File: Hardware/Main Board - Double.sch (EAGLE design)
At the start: 69 parts, among them J1 MICROMOD-2222-C, J10 MICRO-SD-PUSH-PUSH-EXT-PIN, J2 Vertical Qwiic Connector, J4 QWIIC_RIGHT_ANGLE, J5 CORTEX_JTAG_DEBUG_MINIMUM_PTH, J6 MICROMOD_CARRIER, J7 MICROMOD_CARRIER, Q1 3.1A/30V/105mΩ, U2 MCP73831, U5 AP7361C-33

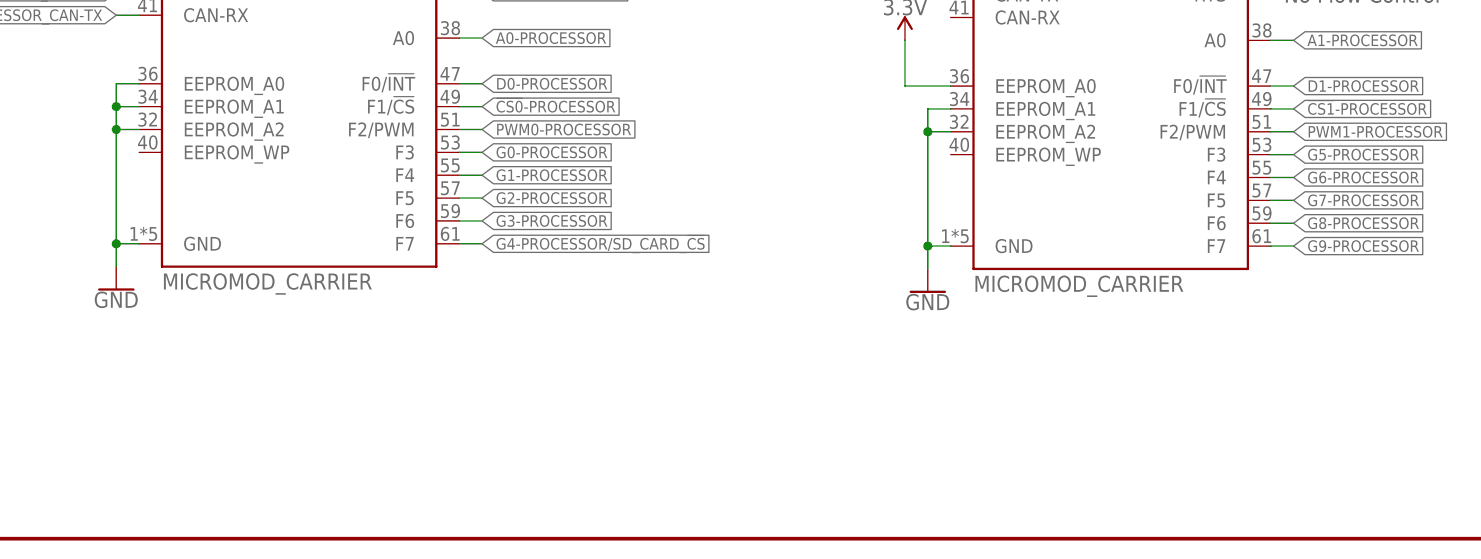
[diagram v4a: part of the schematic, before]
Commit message: Updates the design to use the Micromod-function device in the official SFE Eagle Libs
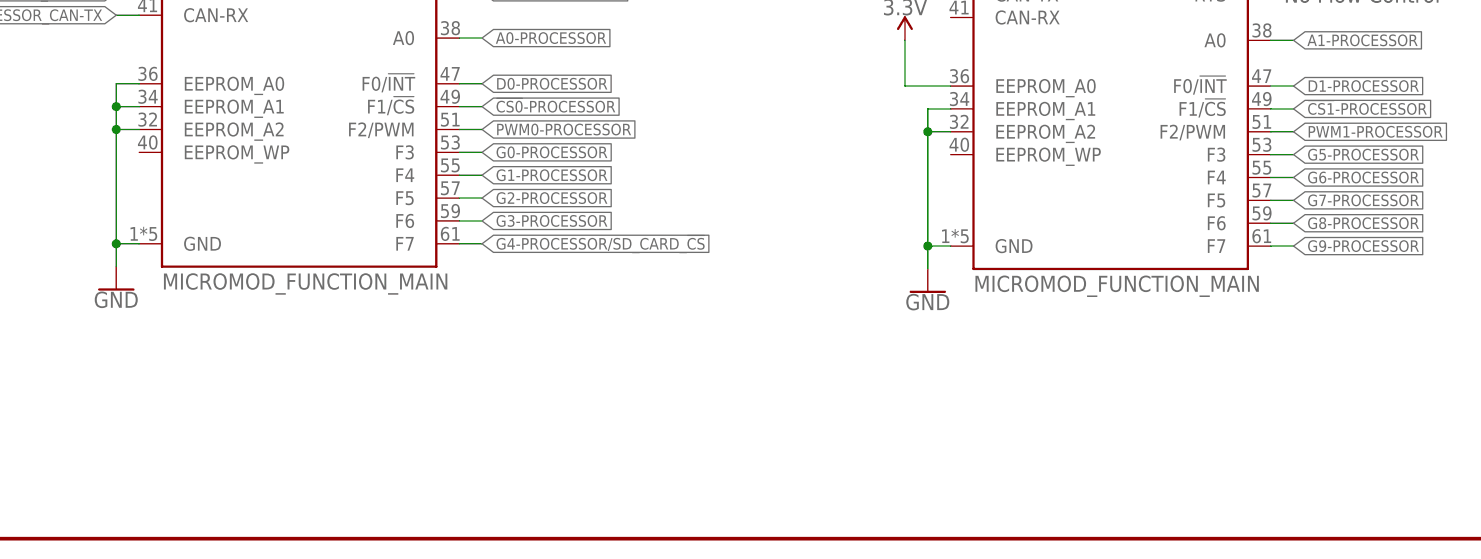
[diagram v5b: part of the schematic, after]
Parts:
- J6, J7: value MICROMOD_CARRIER -> MICROMOD_FUNCTION_MAIN; device SparkFun-MicroMod-Function:MICROMOD_CARRIER -> SparkFun-MicroMod:MICROMOD_FUNCTION_MAIN
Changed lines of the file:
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@@
 <?xml version="1.0" encoding="utf-8"?>
 <!DOCTYPE eagle SYSTEM "eagle.dtd">
-<eagle version="9.6.2">
+<eagle version="9.5.1">
 <drawing>
 <settings>
@@
 <part name="R10" library="SparkFun-Resistors" deviceset="20KOHM" device="-0603-1/10W-1%" value="20k"/>
 <part name="GND23" library="SparkFun-PowerSymbols" deviceset="GND" device=""/>
-<part name="J6" library="SparkFun-MicroMod-Function" deviceset="MICROMOD" device="_CARRIER" value="MICROMOD_CARRIER"/>
-<part name="J7" library="SparkFun-MicroMod-Function" deviceset="MICROMOD" device="_CARRIER" value="MICROMOD_CARRIER"/>
+<part name="J6" library="SparkFun-MicroMod" deviceset="MICROMOD_FUNCTION" device="_MAIN" value="MICROMOD_FUNCTION_MAIN"/>
+<part name="J7" library="SparkFun-MicroMod" deviceset="MICROMOD_FUNCTION" device="_MAIN" value="MICROMOD_FUNCTION_MAIN"/>
 <part name="SUPPLY2" library="SparkFun-PowerSymbols" deviceset="3.3V" device=""/>
 <part name="J10" library="SparkFun-Connectors" deviceset="MICRO-SD" device="-PUSH-PUSH-EXT-PIN"/>

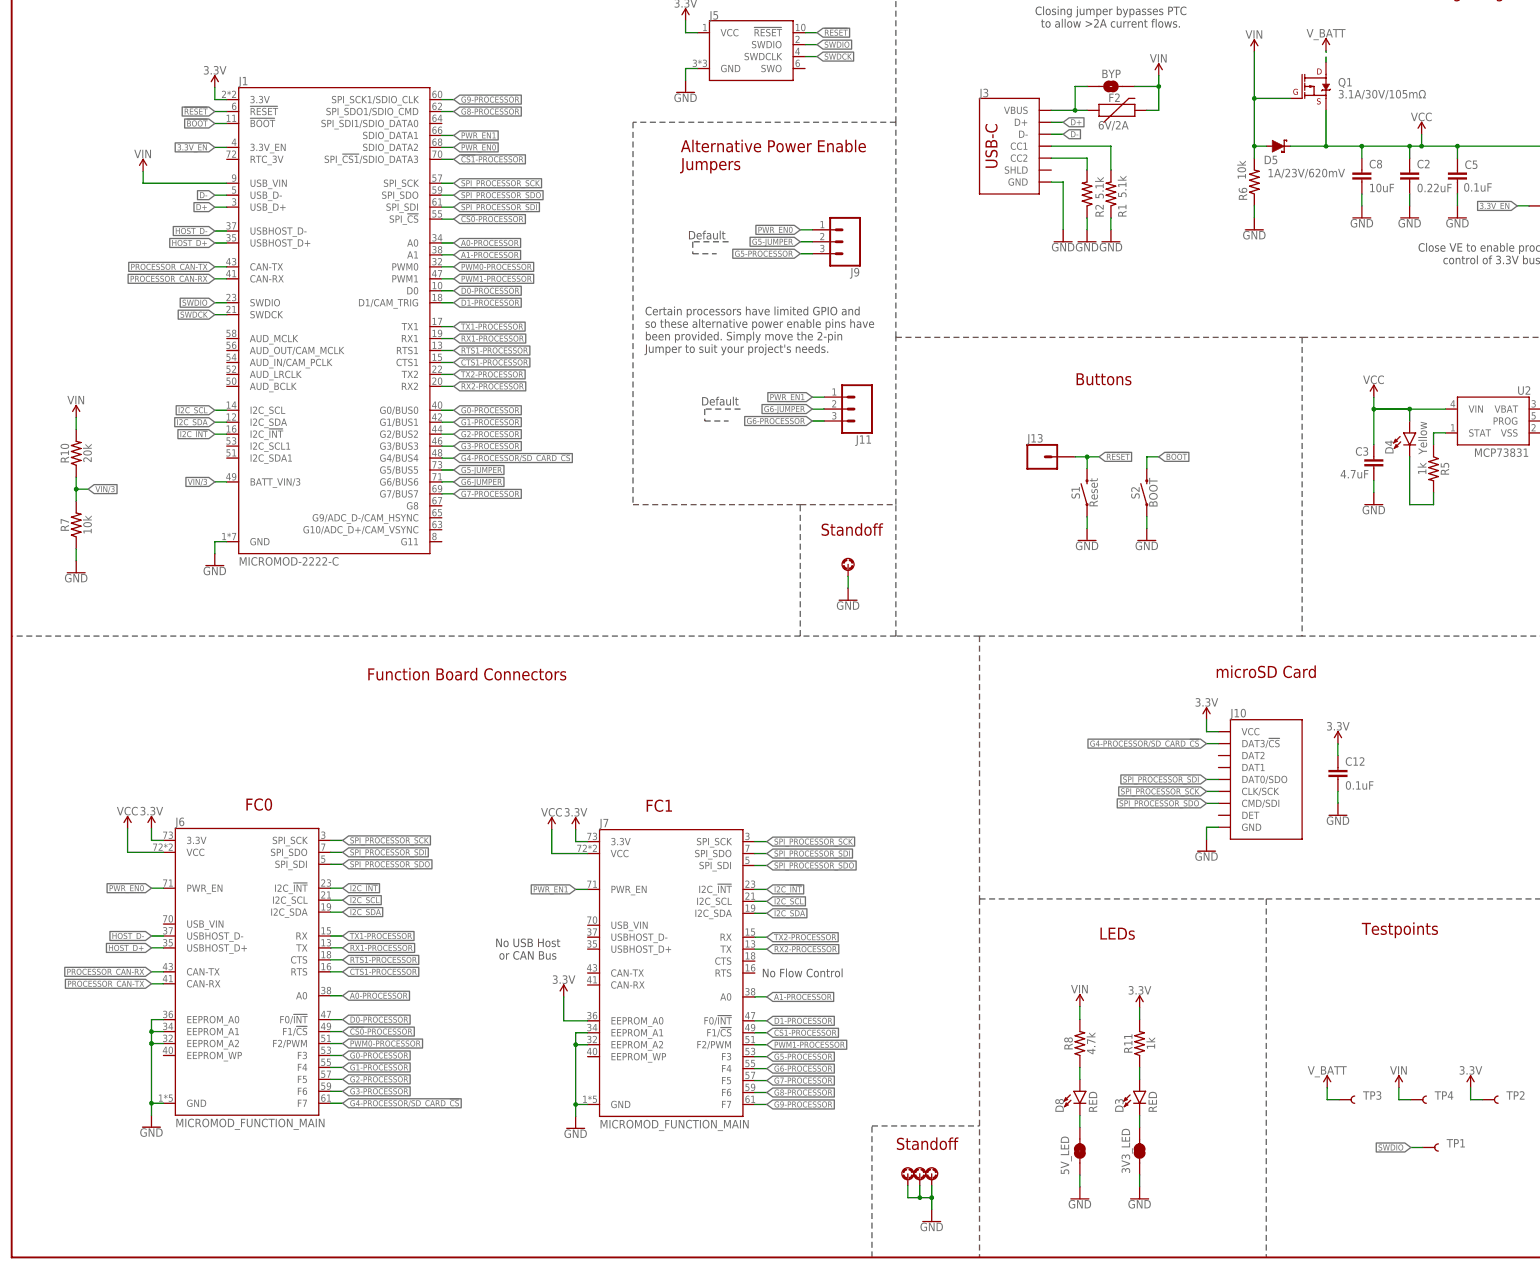
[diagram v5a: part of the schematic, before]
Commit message: Changes resistor values on LEDs, updates plexing symbol, increases capacitor value on microSD
* Adds NC jumper to shield pin on USB-C
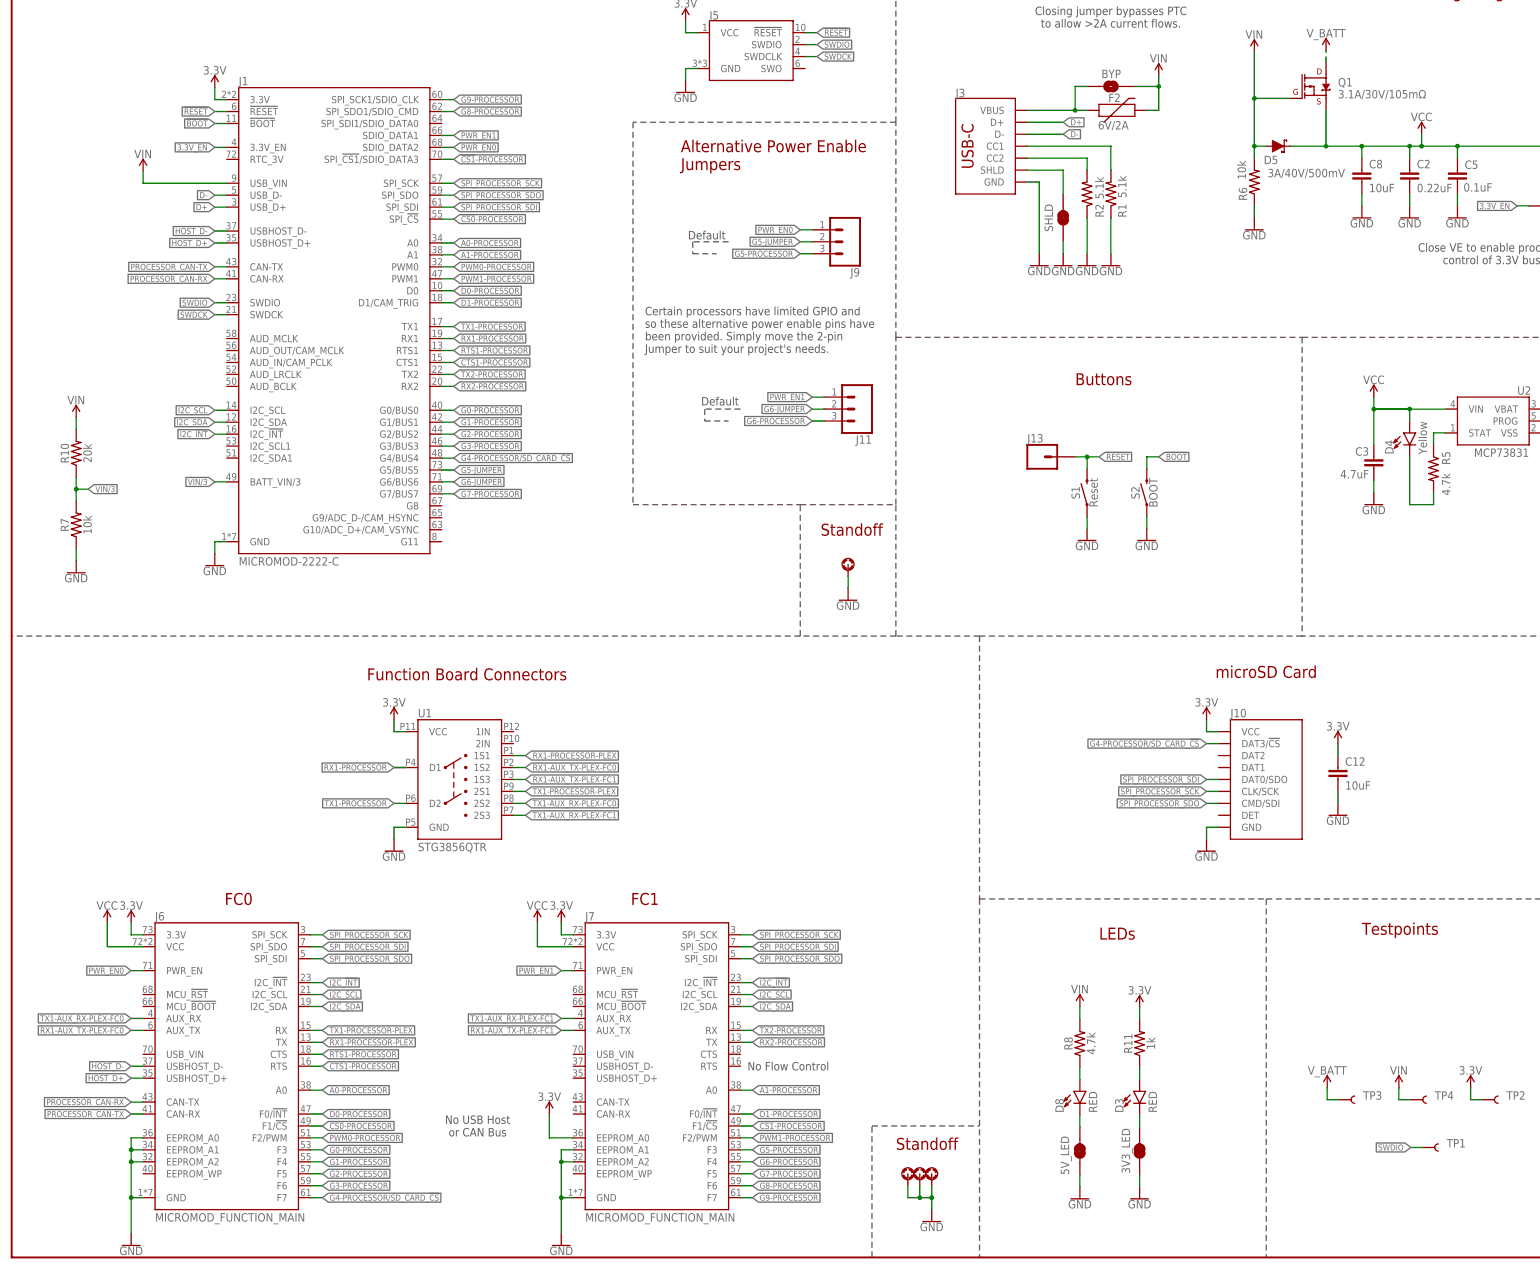
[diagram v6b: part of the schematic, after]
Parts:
- added SHLD: JUMPER-SMT_2_NC_TRACE_SILK, SparkFun-Jumpers:JUMPER-SMT_2_NC_TRACE_SILK
- added U1: STG3856QTR, dip_switch:STG3856QTR
- C12: value 0.1uF -> 10uF; device SparkFun-Capacitors:0.1UF-0603-25V-(+80/-20%) -> SparkFun-Capacitors:10UF-0603-6.3V-20%
- D5: value 1A/23V/620mV -> 3A/40V/500mV; device SparkFun-DiscreteSemi:DIODE-SCHOTTKY-BAT20J -> SparkFun-DiscreteSemi:DIODE-SCHOTTKY-B340A
- R5: value 1k -> 4.7k; device SparkFun-Resistors:1KOHM-0603-1/10W-1% -> SparkFun-Resistors:4.7KOHM-0603-1/10W-1%
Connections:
- new net N$11: J3.SHLD, SHLD.2
- new net N$16: U1.1IN
- new net N$17: U1.2IN
- new net RX1-AUX_TX-PLEX-FC0: J6.AUX_TX, U1.1S2
- new net RX1-AUX_TX-PLEX-FC1: J7.AUX_TX, U1.1S3
- new net RX1-PROCESSOR-PLEX: J6.TX, U1.1S1
- new net TX1-AUX_RX-PLEX-FC0: J6.AUX_RX, U1.2S2
- new net TX1-AUX_RX-PLEX-FC1: J7.AUX_RX, U1.2S3
- new net TX1-PROCESSOR-PLEX: J6.RX, U1.2S1
- net 3.3V: now also U1.VCC
- net GND: now also SHLD.1, U1.GND
- net RX1-PROCESSOR: now also U1.D1; no longer J6.TX
- net TX1-PROCESSOR: now also U1.D2; no longer J6.RX
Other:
- moved on the sheet: J3
